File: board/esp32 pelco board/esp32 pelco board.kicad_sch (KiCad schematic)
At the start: 69 parts, among them J1 Conn_02x05_Odd_Even, J10 qwiic, J11 Conn_01x02, J12 from connector, J13 battery bypass, J14 to rest of device, J15 qwiic, J16 qwiic, J2 Conn_02x03_Odd_Even, J3 qwiic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

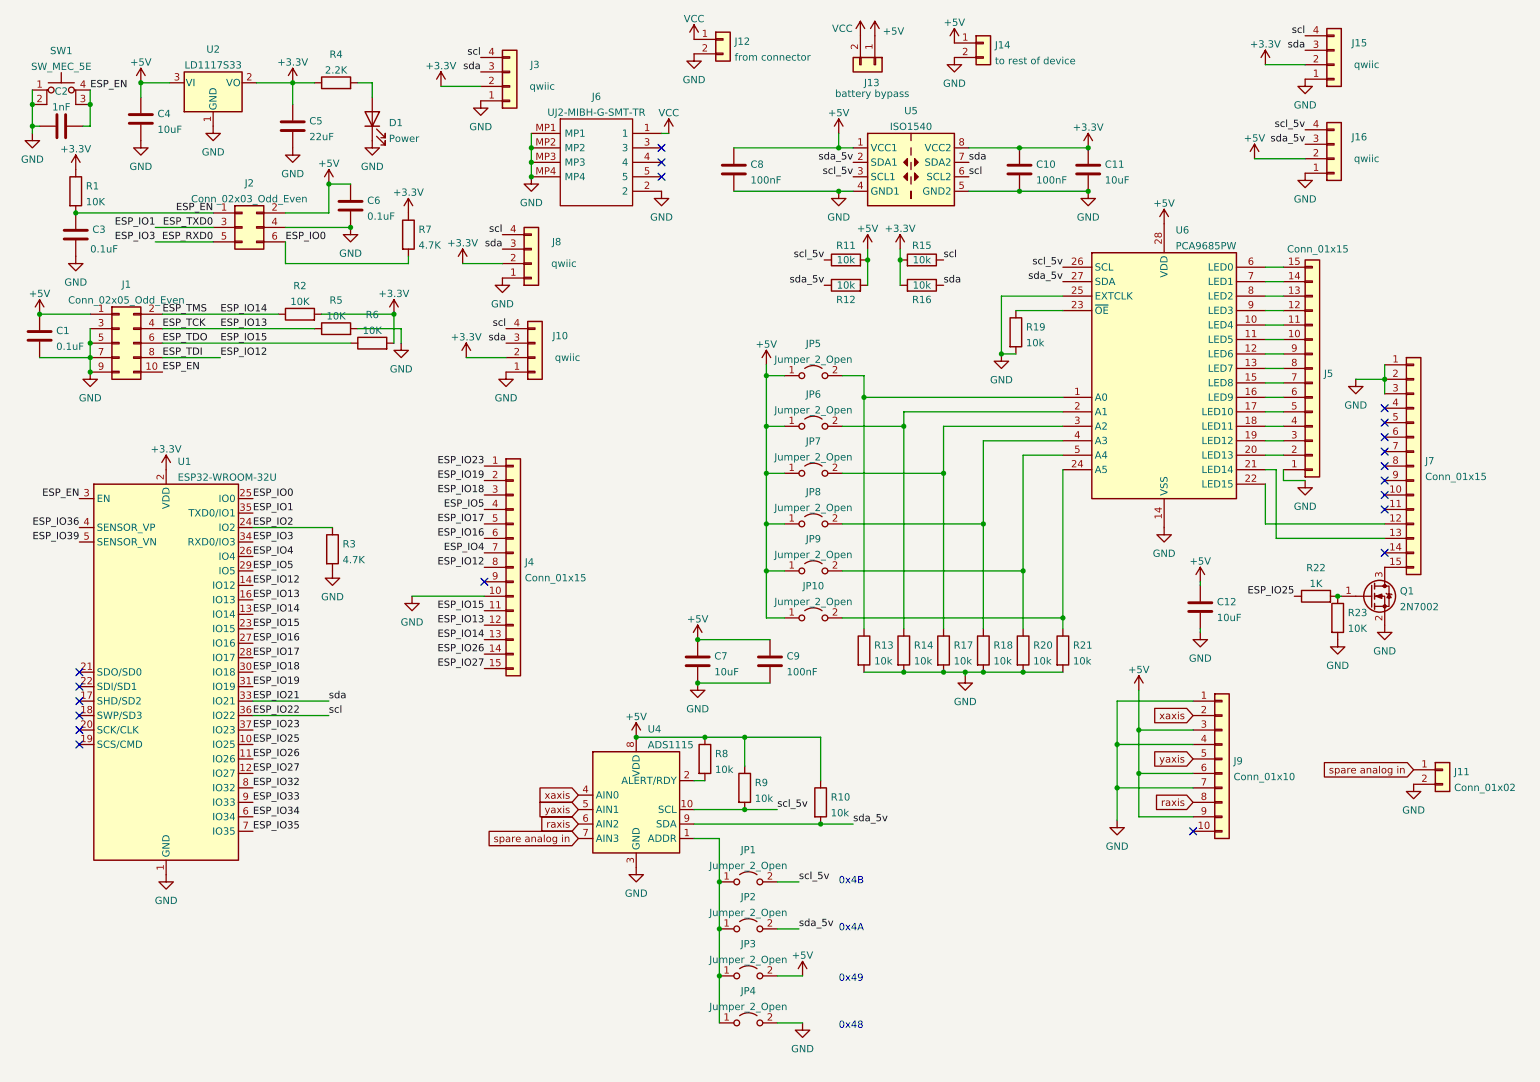
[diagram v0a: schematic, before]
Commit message: added usb serial and programming button
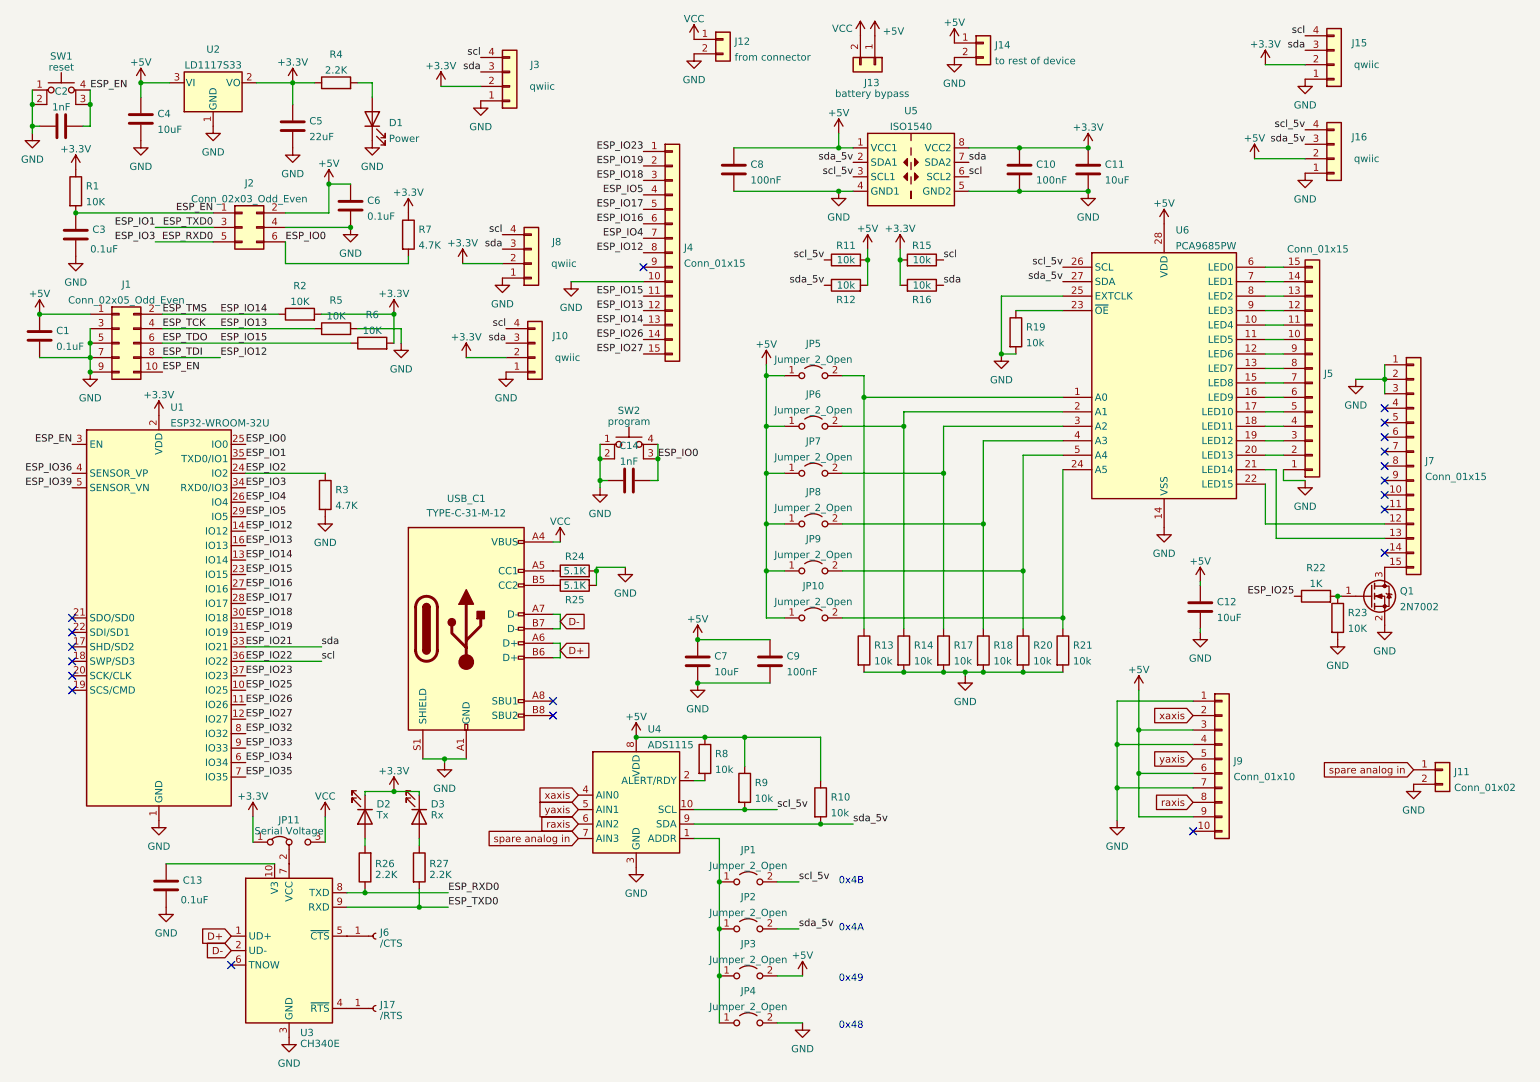
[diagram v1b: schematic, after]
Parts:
- removed J6: UJ2-MIBH-G-SMT-TR, Evan's misc parts:UJ2MIBHGSMTTR, symbol mouser:UJ2-MIBH-G-SMT-TR
- added C13: 0.1uF, Capacitor_SMD:C_0603_1608Metric, symbol Device:C
- added C14: 1nF, Capacitor_SMD:C_0603_1608Metric, symbol Device:C
- added D2: Tx, LED_SMD:LED_0603_1608Metric, symbol Device:LED
- added D3: Rx, LED_SMD:LED_0603_1608Metric, symbol Device:LED
- added J17: /RTS, Connector_PinSocket_2.54mm:PinSocket_1x01_P2.54mm_Vertical, symbol Connector:Conn_01x01_Socket
- added J6: /CTS, Connector_PinSocket_2.54mm:PinSocket_1x01_P2.54mm_Vertical, symbol Connector:Conn_01x01_Socket
- added JP11: Serial Voltage, Jumper:SolderJumper-3_P1.3mm_Bridged12_RoundedPad1.0x1.5mm, symbol Jumper:Jumper_3_Bridged12
- added R24, R25: 5.1K, Resistor_SMD:R_0603_1608Metric, symbol Device:R
- added R26, R27: 2.2K, Resistor_SMD:R_0603_1608Metric, symbol Device:R
- added SW2: program, Button_Switch_THT:SW_TH_Tactile_Omron_B3F-10xx, symbol Switch:SW_MEC_5E
- added U3: CH340E, Package_SO:MSOP-10_3x3mm_P0.5mm, symbol Interface_USB:CH340E
- added USB_C1: TYPE-C-31-M-12, Connector_USB:USB_C_Receptacle_HRO_TYPE-C-31-M-12, symbol Connector:USB_C_Receptacle_USB2.0
- SW1: value SW_MEC_5E -> reset
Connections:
- net +3V3: now also D2.1 (K), D3.1 (K), JP11.1 (A)
- net ESP_IO0: now also C14.2, SW2.3 (K), SW2.4 (A)
- net ESP_IO1: now also R27.2, U3.9 (RXD)
- net ESP_IO3: now also R26.1, U3.8 (TXD)
- net GND: now also C13.2, C14.1, R24.2, R25.2, SW2.1, SW2.2, U3.3 (GND), USB_C1.A1 (GND), USB_C1.A12 (GND), USB_C1.B1 (GND), USB_C1.B12 (GND), USB_C1.S1 (SHIELD)
- net VCC: now also JP11.3 (B), USB_C1.A4 (VBUS), USB_C1.A9 (VBUS), USB_C1.B4 (VBUS), USB_C1.B9 (VBUS)
- new net: R24.1, USB_C1.A5 (CC1)
- new net: R25.1, USB_C1.B5 (CC2)
- new net: D3.2 (A), R27.1
- new net: J6.1 (Pin_1), U3.5 (~{CTS})
- new net: JP11.2 (C), U3.7 (VCC)
- new net: C13.1, U3.10 (V3)
- new net: D2.2 (A), R26.2
- new net: J17.1 (Pin_1), U3.4 (~{RTS})
- new net D+: U3.1 (UD+), USB_C1.A6 (D+), USB_C1.B6 (D+)
- new net D-: U3.2 (UD-), USB_C1.A7 (D-), USB_C1.B7 (D-)
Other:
- moved on the sheet: J4, R3, U1

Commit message: updated gitignore and board tweaks
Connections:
- net +5V: now also J7.4 (Pin_4), J7.5 (Pin_5)
- no-connect marks 20 -> 18
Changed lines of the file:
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@@
   (junction (at 191.135 110.49) (diameter 0) (color 0 0 0 0)
   )
+  (junction (at 254.635 84.455) (diameter 0) (color 0 0 0 0)
+  )
   (junction (at 137.795 173.355) (diameter 0) (color 0 0 0 0)
   )
@@
   (junction (at 142.24 152.4) (diameter 0) (color 0 0 0 0)
   )
+  (junction (at 254.635 74.295) (diameter 0) (color 0 0 0 0)
+  )
   (junction (at 36.195 24.765) (diameter 0) (color 0 0 0 0)
   )
@@
   (no_connect (at 254.635 89.535))
   (no_connect (at 254.635 86.995))
-  (no_connect (at 254.635 84.455))
-  (no_connect (at 254.635 81.915))
   (no_connect (at 24.13 128.905))
   (no_connect (at 24.13 131.445))
@@
     (stroke (width 0) (type default))
   )
+  (wire (pts (xy 254.635 84.455) (xy 254.635 81.915))
+    (stroke (width 0) (type default))
+  )
   (wire (pts (xy 254.635 76.835) (xy 254.635 79.375))
     (stroke (width 0) (type default))
@@
     (stroke (width 0) (type default))
   )
-  (wire (pts (xy 249.555 76.835) (xy 254.635 76.835))
-    (stroke (width 0) (type default))
-  )
   (wire (pts (xy 18.415 73.025) (xy 27.305 73.025))
     (stroke (width 0) (type default))
@@
     (stroke (width 0) (type default))
   )
+  (wire (pts (xy 249.555 84.455) (xy 254.635 84.455))
+    (stroke (width 0) (type default))
+  )
   (wire (pts (xy 190.5 36.195) (xy 202.565 36.195))
     (stroke (width 0) (type default))
@@
     (stroke (width 0) (type default))
   )
+  (wire (pts (xy 249.555 74.295) (xy 254.635 74.295))
+    (stroke (width 0) (type default))
+  )
   (wire (pts (xy 116.84 94.615) (xy 118.11 94.615))
     (stroke (width 0) (type default))
@@
     )
   )
-  (symbol (lib_id "power:GND") (at 249.555 76.835 0) (unit 1)
+  (symbol (lib_id "power:GND") (at 249.555 74.295 0) (unit 1)
     (in_bom yes) (on_board yes) (dnp no) (fields_autoplaced)
-    (property "Reference" "#PWR0127" (at 249.555 83.185 0)
+    (property "Reference" "#PWR0127" (at 249.555 80.645 0)
       (effects (font (size 1.27 1.27)) hide)
     )
-    (property "Value" "GND" (at 249.555 81.3975 0)
+    (property "Value" "GND" (at 249.555 78.8575 0)
       (effects (font (size 1.27 1.27)))
     )
-    (property "Footprint" "" (at 249.555 76.835 0)
+    (property "Footprint" "" (at 249.555 74.295 0)
       (effects (font (size 1.27 1.27)) hide)
     )
-    (property "Datasheet" "" (at 249.555 76.835 0)
+    (property "Datasheet" "" (at 249.555 74.295 0)
       (effects (font (size 1.27 1.27)) hide)
     )
@@
         )
       )
+    )
+  )
+  (symbol (lib_id "power:+5V") (at 249.555 84.455 0) (unit 1)
+    (in_bom yes) (on_board yes) (dnp no) (fields_autoplaced)
+    (property "Reference" "#PWR028" (at 249.555 88.265 0)
+      (effects (font (size 1.27 1.27)) hide)
+    )
+    (property "Value" "+5V" (at 249.555 80.8505 0)
+      (effects (font (size 1.27 1.27)))
+    )
+    (property "Footprint" "" (at 249.555 84.455 0)
+      (effects (font (size 1.27 1.27)) hide)
+    )
+    (property "Datasheet" "" (at 249.555 84.455 0)
+      (effects (font (size 1.27 1.27)) hide)
+    )
+    (pin "1")
+    (instances
+      (project "esp32 pelco board"
+        (path "/e63e39d7-6ac0-4ffd-8aa3-1841a4541b55"
+          (reference "#PWR028") (unit 1)
+        )
+      )
